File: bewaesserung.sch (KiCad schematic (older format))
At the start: 28 parts, among them J1 vom Raspberry Pi, J2 Ventil GPIO 2, J3 Ventil GPIO 3, J4 Ventil GPIO 15, J5 Netzanschluss 230V AC, K1 PE014005, K2 PE014005, K3 PE014005, K4 PE014005, Q1 IRLML0100, Q2 IRLML0100, Q3 IRLML0100, Q4 IRLML0100, T1 VC10_1_24

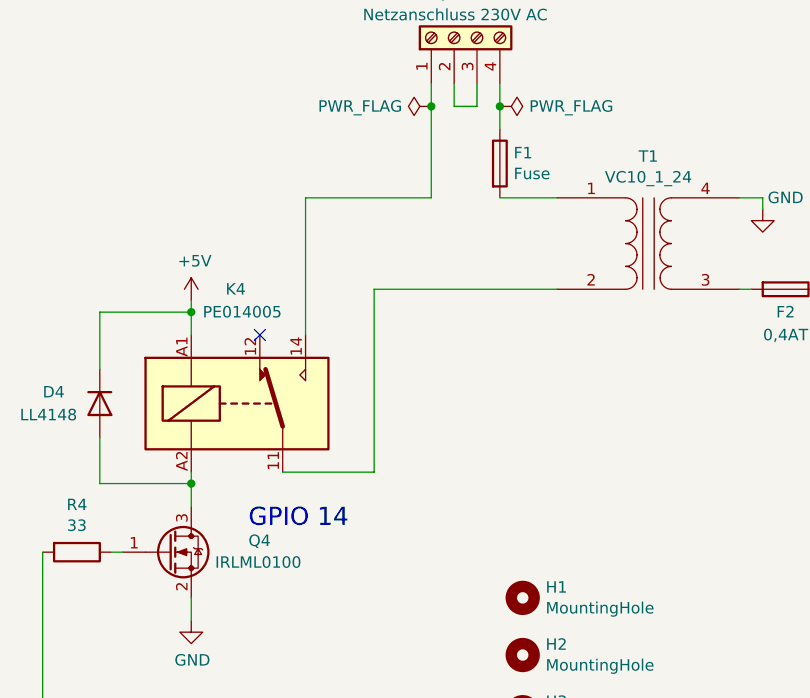
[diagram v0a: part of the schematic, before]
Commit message: Sicherungen angepasst
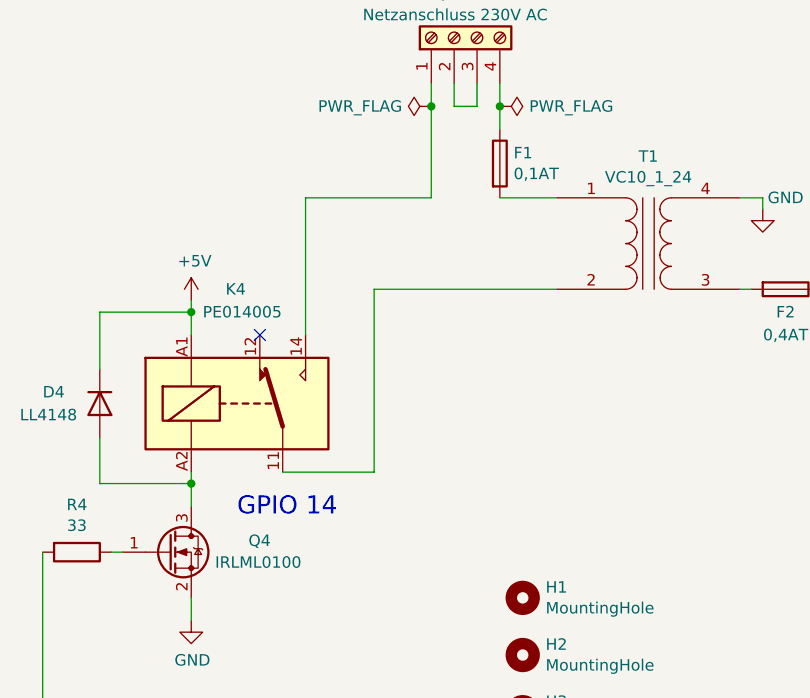
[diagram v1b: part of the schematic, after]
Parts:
- F1: value Fuse -> 0,1AT
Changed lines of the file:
@@
 EESchema Schematic File Version 4
-LIBS:bewaesserung-cache
 EELAYER 30 0
 EELAYER END
@@
 P 8700 2650
 F 0 "F1" H 8760 2696 50  0000 L CNN
-F 1 "Fuse" H 8760 2605 50  0000 L CNN
+F 1 "0,1AT" H 8760 2605 50  0000 L CNN
 F 2 "Gerold:Fuse_TR5" V 8630 2650 50  0001 C CNN
 F 3 "~" H 8700 2650 50  0001 C CNN
@@
 	1    0    0    -1
 $EndComp
-Text Notes 7600 4250 0    79   ~ 0
+Text Notes 7550 4200 0    79   ~ 0
 GPIO 14
 Wire Wire Line
